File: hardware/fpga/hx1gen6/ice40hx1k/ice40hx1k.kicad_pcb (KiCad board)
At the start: 2 copper layers, 52 parts, among them J3 Conn_01x20_Male, U1 LTC3406ES5, U5 AT25SF081-SSHD-X, U6 ICE40HX1K-VQ100(VQFP100), X2 ASE-10MHz, X3 ASE-10MHz, X4 ASE-10MHz, X5 ASV-xxxMHz, X6 ASV-xxxMHz, X7 ASV-xxxMHz

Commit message: preparing FSK and phase experiments: started HX1K gen6 brd
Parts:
- removed C1: 4.7uF, Capacitor_SMD:C_0402_1005Metric
- removed C10, C11, C12, C13, C14, C15, C16, C17, C18, C19, C20, C21, C22, C23, C24: 0.1uF, Capacitor_SMD:C_0402_1005Metric
- removed C2: 10uF, Capacitor_SMD:C_0603_1608Metric
- removed C3: 1uF, Capacitor_SMD:C_0402_1005Metric
- removed C31, C32, C33, C34, C35, C36: 0.01uF, Capacitor_SMD:C_0402_1005Metric
- removed D1, D2, D3, D4: LED, LED_SMD:LED_1206_3216Metric
- removed D5: CDBU05, Capacitor_SMD:C_0603_1608Metric
- removed J3: Conn_01x20_Male, Connector_PinHeader_2.54mm:PinHeader_1x20_P2.54mm_Vertical
- removed L1: 2.2uH, Inductor_SMD:L_0805_2012Metric
- removed R1, R2: 100kOhm, Resistor_SMD:R_0402_1005Metric
- removed R10, R5, R6, R7, R8, R9: 10kOhm, Resistor_SMD:R_0402_1005Metric
- removed R11, R12, R13, R14: 10kohm, Resistor_SMD:R_0402_1005Metric
- removed U1: LTC3406ES5, Package_TO_SOT_SMD:TSOT-23-5
- removed U5: AT25SF081-SSHD-X, Package_SO:SOIC-8_3.9x4.9mm_P1.27mm
- removed U6: ICE40HX1K-VQ100(VQFP100), Package_QFP:LQFP-100_14x14mm_P0.5mm
- removed X2, X3, X4: ASE-10MHz, Oscillator:Oscillator_SMD_Abracon_ASE-4Pin_3.2x2.5mm
- removed X5, X6, X7: ASV-xxxMHz, Oscillator:Oscillator_SMD_Abracon_ASV-4Pin_7.0x5.1mm
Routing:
- removed copper zone on B.Cu, net GND
- removed copper zone on F.Cu, net GND

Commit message: preparing FSK and phase experiments: started HX1K gen6 brd
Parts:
- added C1: 0.1uF, Capacitor_SMD:C_0402_1005Metric, F.Cu at (165.0, 91.3)
- added C10: 0.1uF, Capacitor_SMD:C_0402_1005Metric, F.Cu at (194.4, 57.8)
- added C11: 0.1uF, Capacitor_SMD:C_0402_1005Metric, F.Cu at (201.3, 51.3)
- added C12: 0.1uF, Capacitor_SMD:C_0402_1005Metric, F.Cu at (197.3, 53.8)
- added C13: 0.1uF, Capacitor_SMD:C_0402_1005Metric, F.Cu at (194.4, 53.8)
- added C14: 0.1uF, Capacitor_SMD:C_0402_1005Metric, F.Cu at (194.4, 55.8)
- added C15: 0.1uF, Capacitor_SMD:C_0402_1005Metric, F.Cu at (198.4, 51.3)
- added C16: 0.01uF, Capacitor_SMD:C_0402_1005Metric, F.Cu at (181.0, 77.6)
- added C17: 0.01uF, Capacitor_SMD:C_0402_1005Metric, F.Cu at (186.1, 73.2)
- added C18: 0.01uF, Capacitor_SMD:C_0402_1005Metric, F.Cu at (181.0, 79.6)
- added C19: 4.7uF, Capacitor_SMD:C_0402_1005Metric, F.Cu at (198.3, 113.1)
- added C2: 0.1uF, Capacitor_SMD:C_0402_1005Metric, F.Cu at (194.4, 61.7)
- added C20: 10uF, Capacitor_SMD:C_0603_1608Metric, F.Cu at (195.9, 110.9)
- added C21: 0.1uF, Capacitor_SMD:C_0402_1005Metric, F.Cu at (79.7, 118.3)
- added C22: 4.7uF, Capacitor_SMD:C_0402_1005Metric, F.Cu at (82.6, 118.3)
- added C23: 0.1uF, Capacitor_SMD:C_0402_1005Metric, F.Cu at (82.6, 116.3)
- added C24: 4.7uF, Capacitor_SMD:C_0402_1005Metric, F.Cu at (193.7, 118.6)
- added C25: 10uF, Capacitor_SMD:C_0603_1608Metric, F.Cu at (191.4, 116.4)
- added C3: 0.1uF, Capacitor_SMD:C_0402_1005Metric, F.Cu at (203.1, 53.3)
- added C4: 0.1uF, Capacitor_SMD:C_0402_1005Metric, F.Cu at (197.3, 57.8)
- added C5: 0.1uF, Capacitor_SMD:C_0402_1005Metric, F.Cu at (200.2, 55.2)
- added C6: 0.1uF, Capacitor_SMD:C_0402_1005Metric, F.Cu at (204.2, 51.3)
- added C7: 0.1uF, Capacitor_SMD:C_0402_1005Metric, F.Cu at (194.4, 59.7)
- added C8: 0.1uF, Capacitor_SMD:C_0402_1005Metric, F.Cu at (200.2, 53.3)
- added C9: 0.1uF, Capacitor_SMD:C_0402_1005Metric, F.Cu at (197.3, 55.8)
- added D1: CDBU05, Capacitor_SMD:C_0603_1608Metric, F.Cu at (195.0, 51.6)
- added D2: LED, LED_SMD:LED_1206_3216Metric, F.Cu at (154.7, 106.5)
- added D3: LED, LED_SMD:LED_1206_3216Metric, F.Cu at (126.9, 87.8)
- added D4: LED, LED_SMD:LED_1206_3216Metric, F.Cu at (121.2, 91.2)
- added D5: LED, LED_SMD:LED_1206_3216Metric, F.Cu at (121.2, 87.8)
- added J1: Conn_01x06_Male, Connector_PinHeader_2.54mm:PinHeader_1x06_P2.54mm_Vertical, F.Cu at (76.0, 110.7)
- added J2: Conn_01x20_Male, Connector_PinHeader_2.54mm:PinHeader_1x20_P2.54mm_Horizontal, F.Cu at (109.0, 101.8)
- added J3: Conn_01x20_Male, Connector_PinHeader_2.54mm:PinHeader_1x20_P2.54mm_Horizontal, F.Cu at (120.4, 47.0)
- added L1: 2.2uH, Inductor_SMD:L_0805_2012Metric, F.Cu at (191.7, 113.8)
- added L2: 2.2uH, Inductor_SMD:L_0805_2012Metric, F.Cu at (191.7, 111.0)
- added R1: 10kOhm, Resistor_SMD:R_0402_1005Metric, F.Cu at (162.1, 87.3)
- added R10: 10kohm, Resistor_SMD:R_0402_1005Metric, F.Cu at (131.1, 91.1)
- added R11: 10kohm, Resistor_SMD:R_0402_1005Metric, F.Cu at (131.1, 89.1)
- added R12: 10kohm, Resistor_SMD:R_0402_1005Metric, F.Cu at (131.1, 87.1)
- added R13: 10kOhm, Resistor_SMD:R_0402_1005Metric, F.Cu at (79.8, 116.3)
- added R15: 100kOhm, Resistor_SMD:R_0402_1005Metric, F.Cu at (190.8, 118.6)
- added R16: 450kOhm, Resistor_SMD:R_0402_1005Metric, F.Cu at (194.8, 116.1)
- added R2: 10kOhm, Resistor_SMD:R_0402_1005Metric, F.Cu at (162.1, 89.3)
- added R3: 10kOhm, Resistor_SMD:R_0402_1005Metric, F.Cu at (165.0, 87.3)
- added R4: 10kOhm, Resistor_SMD:R_0402_1005Metric, F.Cu at (162.1, 91.3)
- added R5: 10kOhm, Resistor_SMD:R_0402_1005Metric, F.Cu at (165.0, 89.3)
- added R6: 10kOhm, Resistor_SMD:R_0402_1005Metric, F.Cu at (162.1, 93.3)
- added R7: 100kOhm, Resistor_SMD:R_0402_1005Metric, F.Cu at (199.4, 110.6)
- added R8: 100kOhm, Resistor_SMD:R_0402_1005Metric, F.Cu at (195.4, 113.1)
- added R9: 10kohm, Resistor_SMD:R_0402_1005Metric, F.Cu at (156.5, 111.3)
- added U1: AT25SF081-SSHD-X, Package_SO:SOIC-8_3.9x4.9mm_P1.27mm, F.Cu at (156.4, 89.5)
- added U2: ICE40HX1K-VQ100(VQFP100), Package_QFP:LQFP-100_14x14mm_P0.5mm, F.Cu at (141.9, 71.6)
- added U3: LTC3406ES5, Package_TO_SOT_SMD:TSOT-23-5, F.Cu at (186.7, 116.3)
- added U4: ATSAMD11D14A-M, Package_DFN_QFN:QFN-24-1EP_4x4mm_P0.5mm_EP2.6x2.6mm, F.Cu at (140.1, 106.6)
- added U5: LTC3406ES5, Package_TO_SOT_SMD:TSOT-23-5, F.Cu at (186.7, 111.8)
- added X1: ASE-10MHz, Oscillator:Oscillator_SMD_Abracon_ASE-4Pin_3.2x2.5mm, F.Cu at (177.0, 74.4)
- added X2: ASE-10MHz, Oscillator:Oscillator_SMD_Abracon_ASE-4Pin_3.2x2.5mm, F.Cu at (177.0, 78.8)
- added X3: ASE-10MHz, Oscillator:Oscillator_SMD_Abracon_ASE-4Pin_3.2x2.5mm, F.Cu at (182.1, 74.4)
- added X4: USBFCI_10103594_MILL, kifootp:FCI_10103594_MILL, F.Cu at (82.8, 114.6)

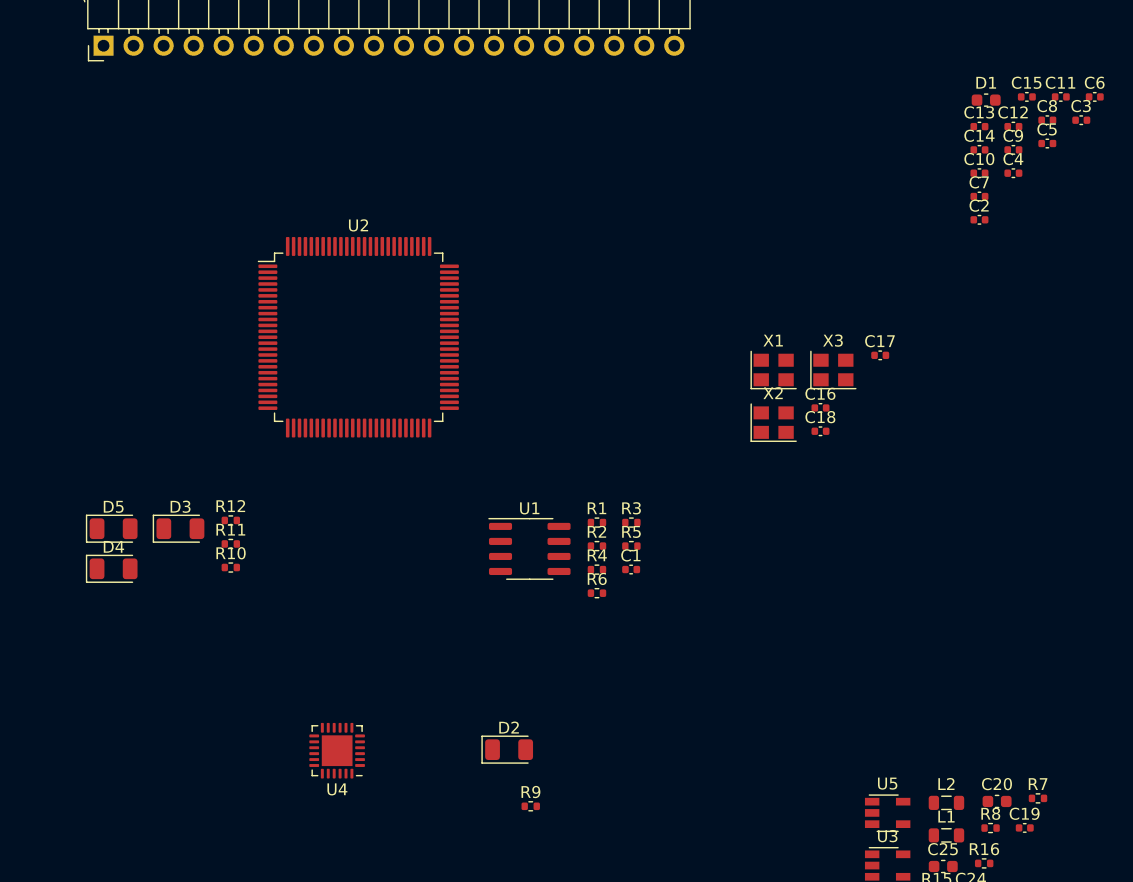
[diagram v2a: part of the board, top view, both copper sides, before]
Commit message: preparing FSK and phase experiments: started HX1K gen6 brd
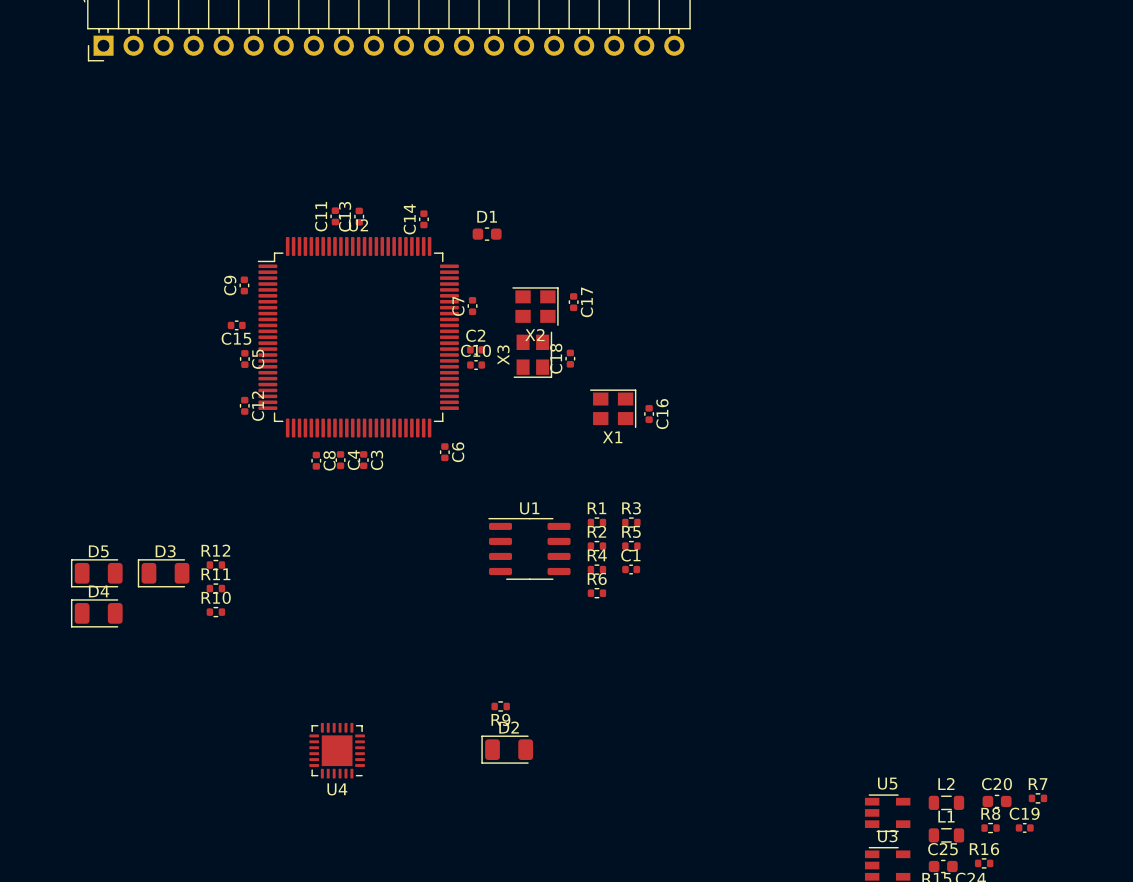
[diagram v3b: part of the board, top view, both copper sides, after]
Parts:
- moved C5 70.3 mm to (132.3, 73.5), turned to 270 degrees
- moved C15 69.5 mm to (131.6, 70.6), turned to 180 degrees
- moved C12 69.1 mm to (132.3, 77.4), turned to 270 degrees
- moved C8 68.2 mm to (138.4, 82.1), turned to 270 degrees
- moved C3 67.1 mm to (142.4, 82.0), turned to 270 degrees
- moved C9 66.0 mm to (132.3, 67.2), turned to 90 degrees
- moved C6 62.6 mm to (149.2, 81.3), turned to 270 degrees
- moved C11 62.2 mm to (140.0, 61.4), turned to 90 degrees
- moved C4 61.8 mm to (140.4, 82.0), turned to 270 degrees
- moved C13 53.0 mm to (142.0, 61.4), turned to 90 degrees
- moved C14 47.3 mm to (147.5, 61.7), turned to 90 degrees
- moved C10 45.5 mm to (151.9, 74.0)
- moved C2 44.0 mm to (151.9, 72.7)
- moved C7 43.8 mm to (151.6, 69.0), turned to 90 degrees
- moved D1 43.7 mm to (152.8, 62.9)
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
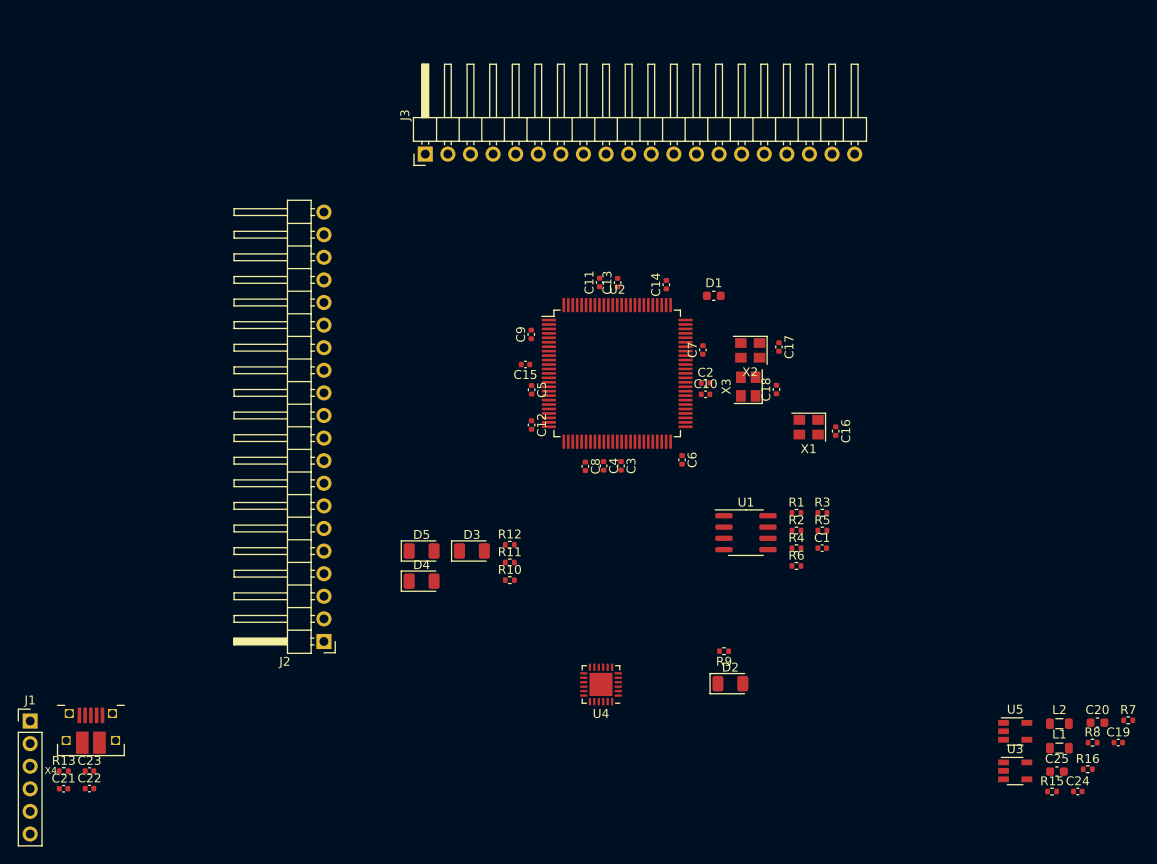
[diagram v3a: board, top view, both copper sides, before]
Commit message: preparing FSK and phase experiments: started HX1K gen6 brd
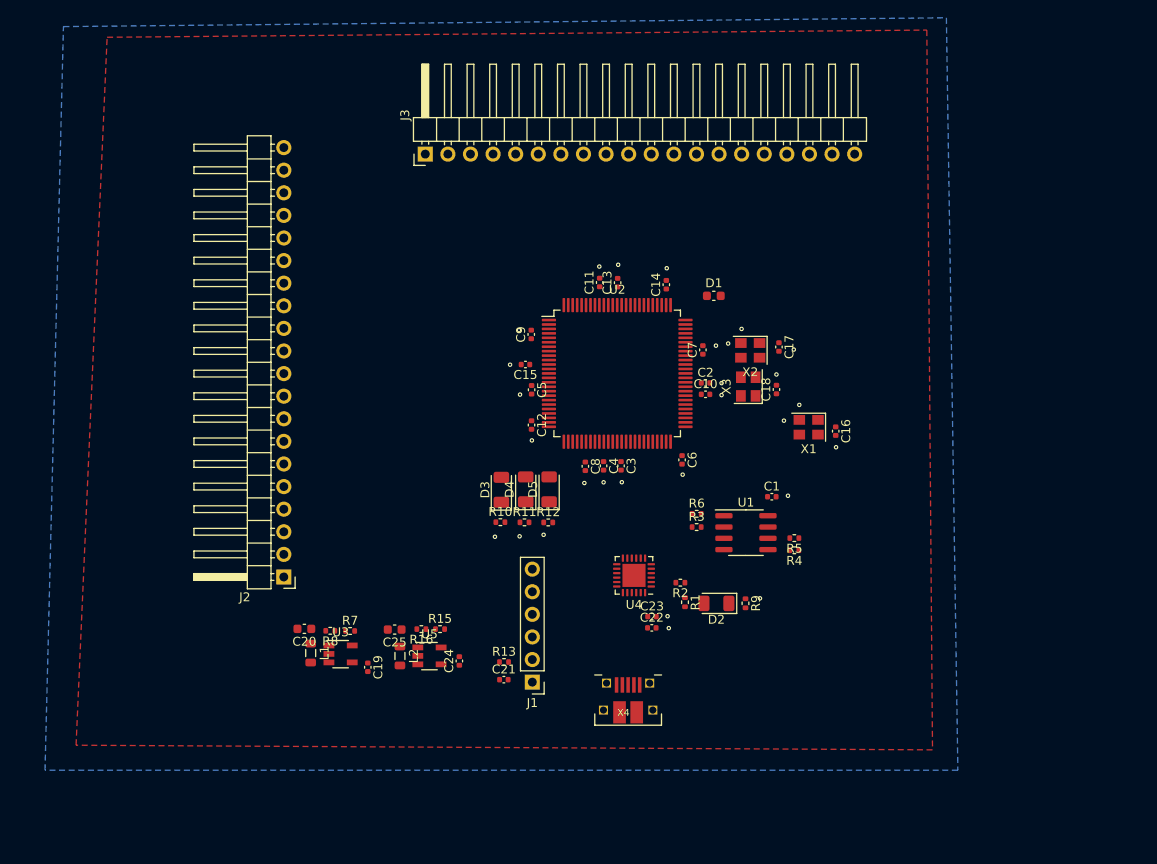
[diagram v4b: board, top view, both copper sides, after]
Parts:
- moved C20 89.8 mm to (106.8, 100.3), turned to 180 degrees
- moved R7 88.0 mm to (111.9, 100.6)
- moved R8 86.6 mm to (109.7, 100.6), turned to 180 degrees
- moved L1 84.8 mm to (107.5, 103.1), turned to 270 degrees
- moved C19 84.8 mm to (113.9, 104.7), turned to 270 degrees
- moved U3 77.0 mm to (110.9, 103.2)
- moved R16 76.5 mm to (119.9, 100.4), turned to 180 degrees
- moved C25 76.1 mm to (116.9, 100.4), turned to 180 degrees
- moved L2 74.5 mm to (117.5, 103.4), turned to 270 degrees
- moved R15 71.2 mm to (122.0, 100.4)
- moved C24 71.0 mm to (124.2, 104.0), turned to 90 degrees
- moved U5 66.4 mm to (120.8, 103.4)
- moved C22 65.7 mm to (145.8, 100.2)
- moved C23 65.6 mm to (145.9, 99.0)
- moved X4 60.5 mm to (143.2, 111.2)
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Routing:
- net GND: vias 0 -> 28
- added copper zone on B.Cu, net GND
- added copper zone on F.Cu, net GND

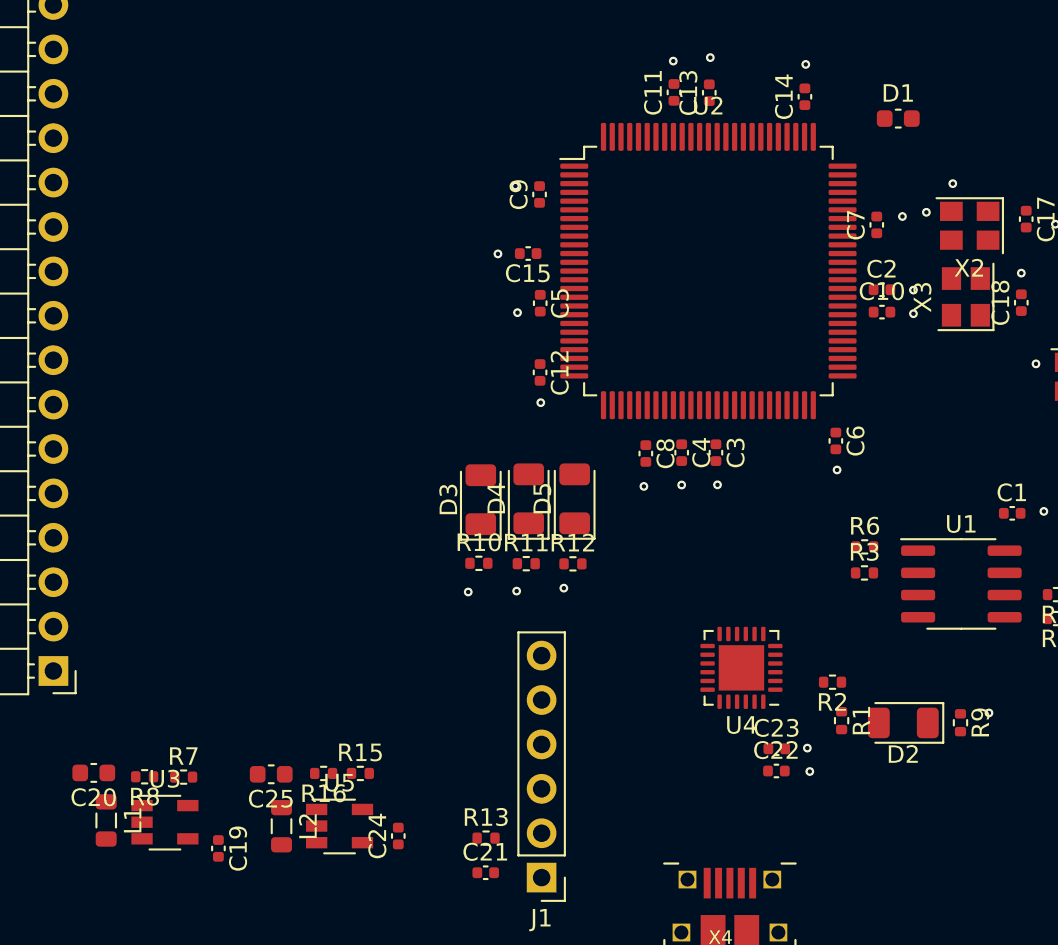
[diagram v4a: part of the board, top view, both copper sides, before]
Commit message: preparing FSK and phase experiments: started HX1K gen6 brd
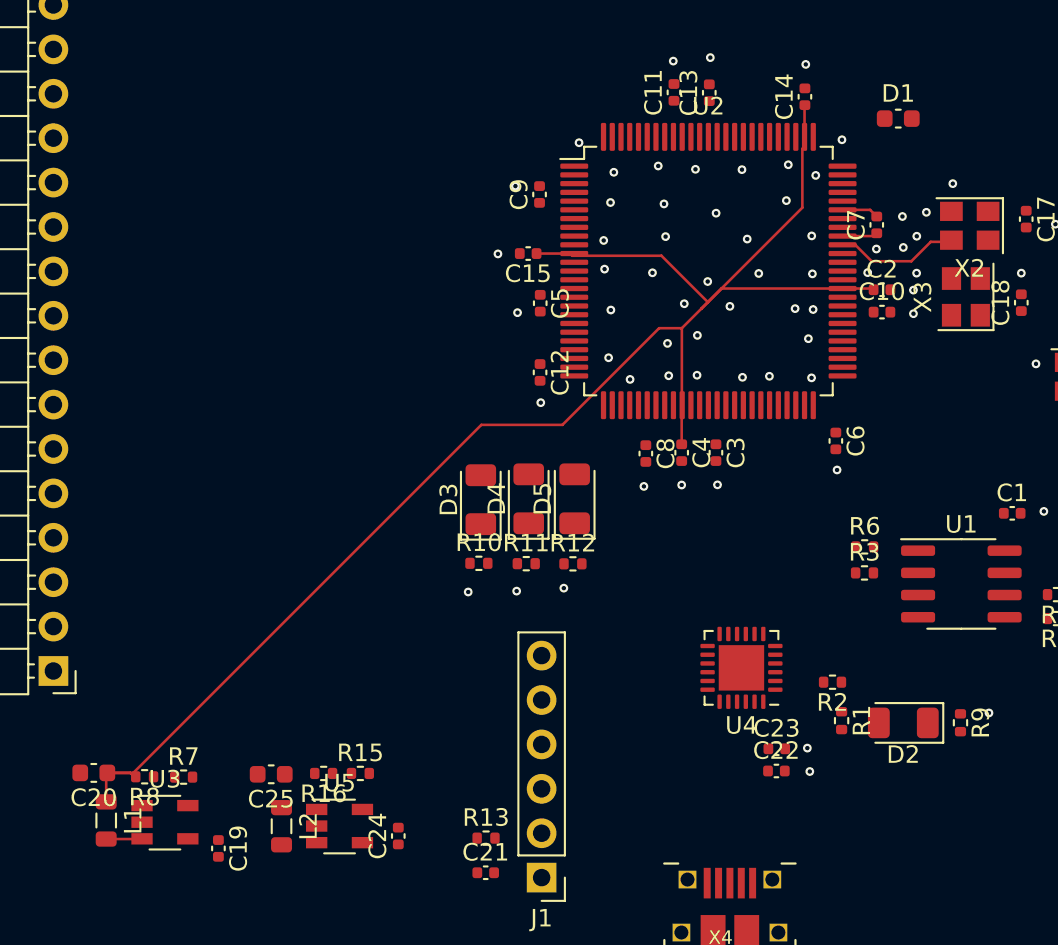
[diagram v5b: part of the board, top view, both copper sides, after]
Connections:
- J2 pad 1: Net-(J2-Pad1) -> GND
- J2 pad 10: IO12_6A -> +3V3
- J2 pad 11: Net-(J2-Pad11) -> GND
- J2 pad 12: Net-(J2-Pad12) -> IO8_3B
- J2 pad 13: IO8_3B -> IO7_3A
- J2 pad 14: IO7_3A -> GND
- J2 pad 15: Net-(J2-Pad15) -> +3V3
- J2 pad 16: Net-(J2-Pad16) -> GND
- J2 pad 19: Net-(J2-Pad19) -> GND
- J2 pad 2: Net-(J2-Pad2) -> IO19_8B
- J2 pad 20: Net-(J2-Pad20) -> +3V3
- J2 pad 3: Net-(J2-Pad3) -> IO18_8A
- J2 pad 4: Net-(J2-Pad4) -> GND
- J2 pad 5: IO19_8B -> +3V3
- J2 pad 6: IO18_8A -> GND
- J2 pad 7: Net-(J2-Pad7) -> IO13_6B
- J2 pad 8: Net-(J2-Pad8) -> IO12_6A
- J2 pad 9: IO13_6B -> GND
- J3 pad 1: Net-(J3-Pad1) -> GND
- J3 pad 11: Net-(J3-Pad11) -> GND
- J3 pad 13: Net-(J3-Pad13) -> GND
- J3 pad 14: Net-(J3-Pad14) -> GND
- J3 pad 15: Net-(J3-Pad15) -> GND
- J3 pad 16: Net-(J3-Pad16) -> GND
- J3 pad 17: Net-(J3-Pad17) -> GND
- J3 pad 18: Net-(J3-Pad18) -> GND
- J3 pad 19: Net-(J3-Pad19) -> GND
- J3 pad 2: Net-(J3-Pad2) -> GND
- J3 pad 20: Net-(J3-Pad20) -> GND
- J3 pad 3: Net-(J3-Pad3) -> GND
- J3 pad 4: Net-(J3-Pad4) -> GND
- J3 pad 5: Net-(J3-Pad5) -> GND
- J3 pad 7: Net-(J3-Pad7) -> GND
- J3 pad 9: Net-(J3-Pad9) -> GND
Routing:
- net +1V2: track 0.00 -> 90.8 mm
- net clock_1: track 0.00 -> 7.09 mm
- net GND: track 0.00 -> 2.07 mm, vias 28 -> 69
- net Net-(L1-Pad2): track 0.00 -> 2.03 mm
- net +3V3: track 0.00 -> 1.97 mm
